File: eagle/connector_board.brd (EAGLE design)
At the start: 22.6 x 24.3 mm, 28 parts, among them IC1 MEGA8-MI, J1 FH12-6S-0.5SH(55), J2 FH12-6S-0.5SH(55), J3 FH12-6S-0.5SH(55), J4 FH12-6S-0.5SH(55), X1 POGOPIN-CONNWITHVIAS-SMV, X2 POGOPIN-CONNWITHVIAS-SMV, X4 POGOPIN-CONNWITHVIAS-SMV, X6 POGOPIN-CONNWITHVIAS-SMV

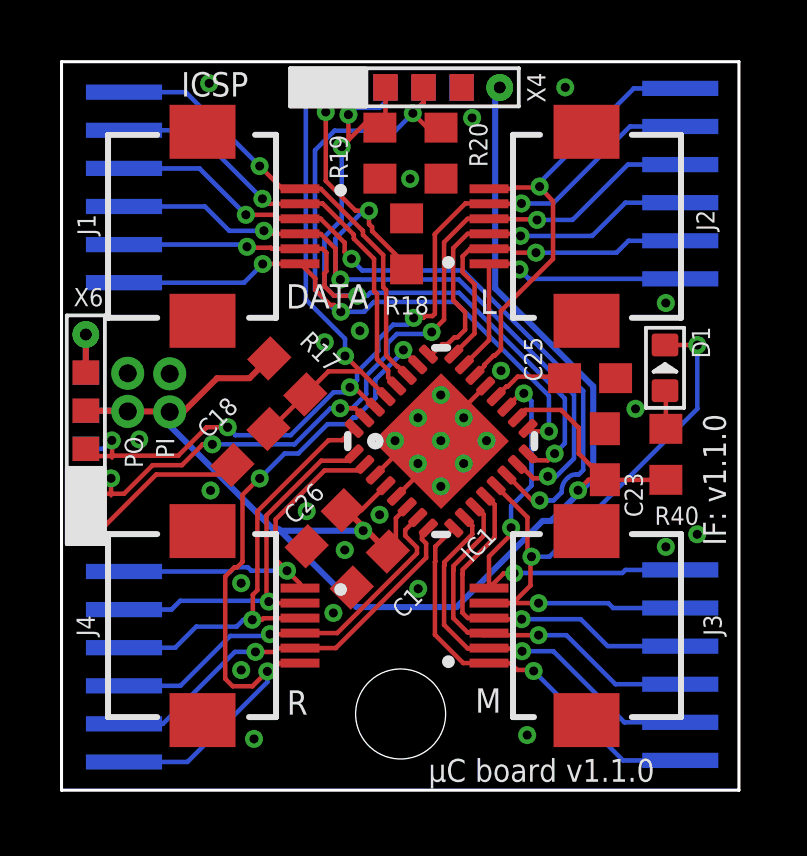
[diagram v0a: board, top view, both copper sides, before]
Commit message: FIX: ICSP pogo prog was missing GND contact on top
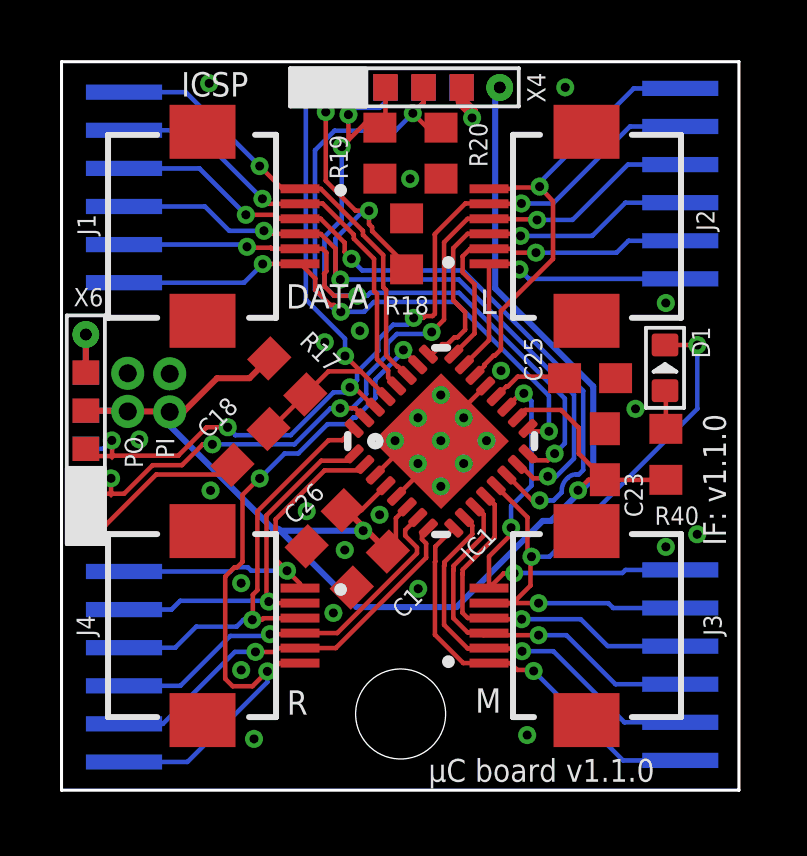
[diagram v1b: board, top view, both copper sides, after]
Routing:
- net GND: track 7.00 -> 8.16 mm
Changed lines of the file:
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@@
 <via x="5.9879625" y="4.00444375" extent="1-16" drill="0.3"/>
 <via x="9.944665625" y="15.312128125" extent="1-16" drill="0.3"/>
-<wire x1="13.335" y1="23.4188" x2="13.337896875" y2="23.4277625" width="0" layer="19" extent="1-16"/>
+<wire x1="13.337896875" y1="23.4277625" x2="13.3432875" y2="23.422371875" width="0.4064" layer="1"/>
+<wire x1="13.3432875" y1="23.422371875" x2="13.3432875" y2="22.94265" width="0.4064" layer="1"/>
+<wire x1="13.6861875" y1="22.59975" x2="13.6861875" y2="22.40925" width="0.4064" layer="1"/>
+<wire x1="13.6861875" y1="22.59975" x2="13.3432875" y2="22.94265" width="0.4064" layer="1"/>
 </signal>
 <signal name="ENCL1A">
